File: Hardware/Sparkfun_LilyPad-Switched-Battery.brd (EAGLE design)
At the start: 31.9 x 30 mm, 13 parts

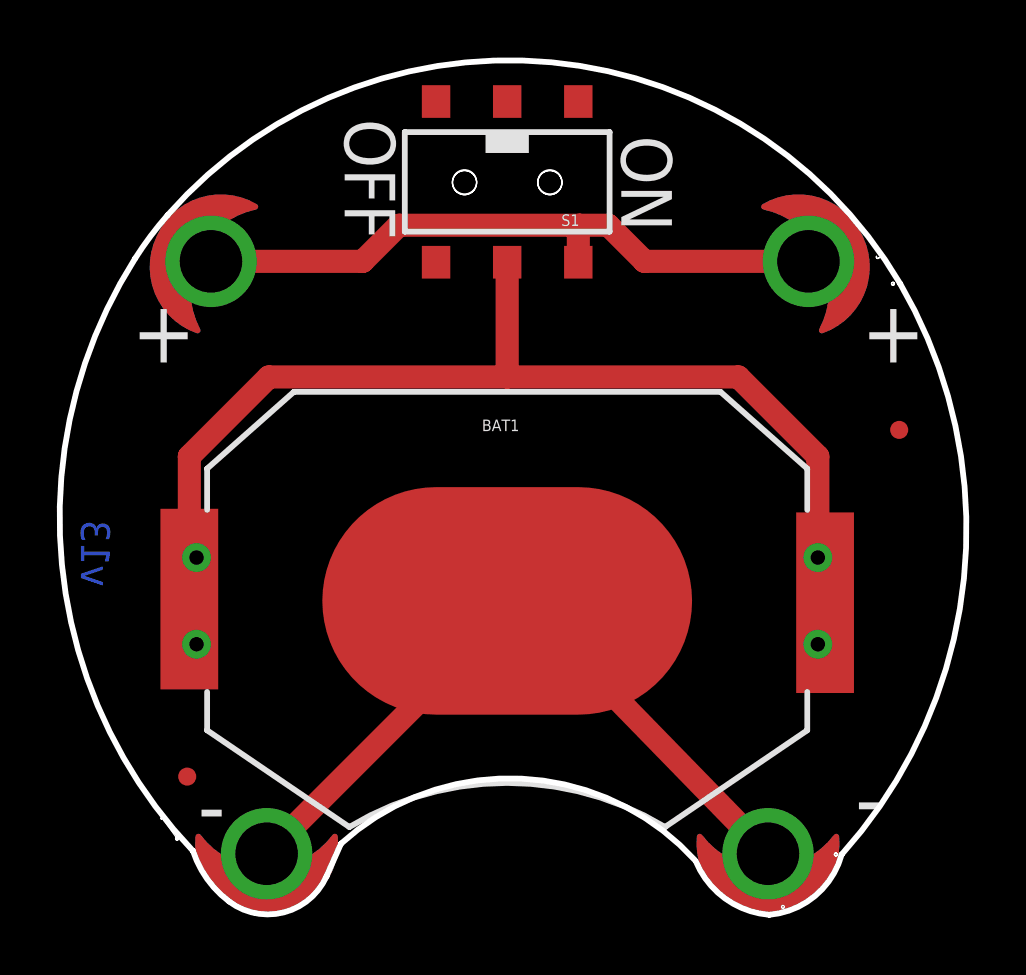
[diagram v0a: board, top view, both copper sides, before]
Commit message: Approved DRC errors
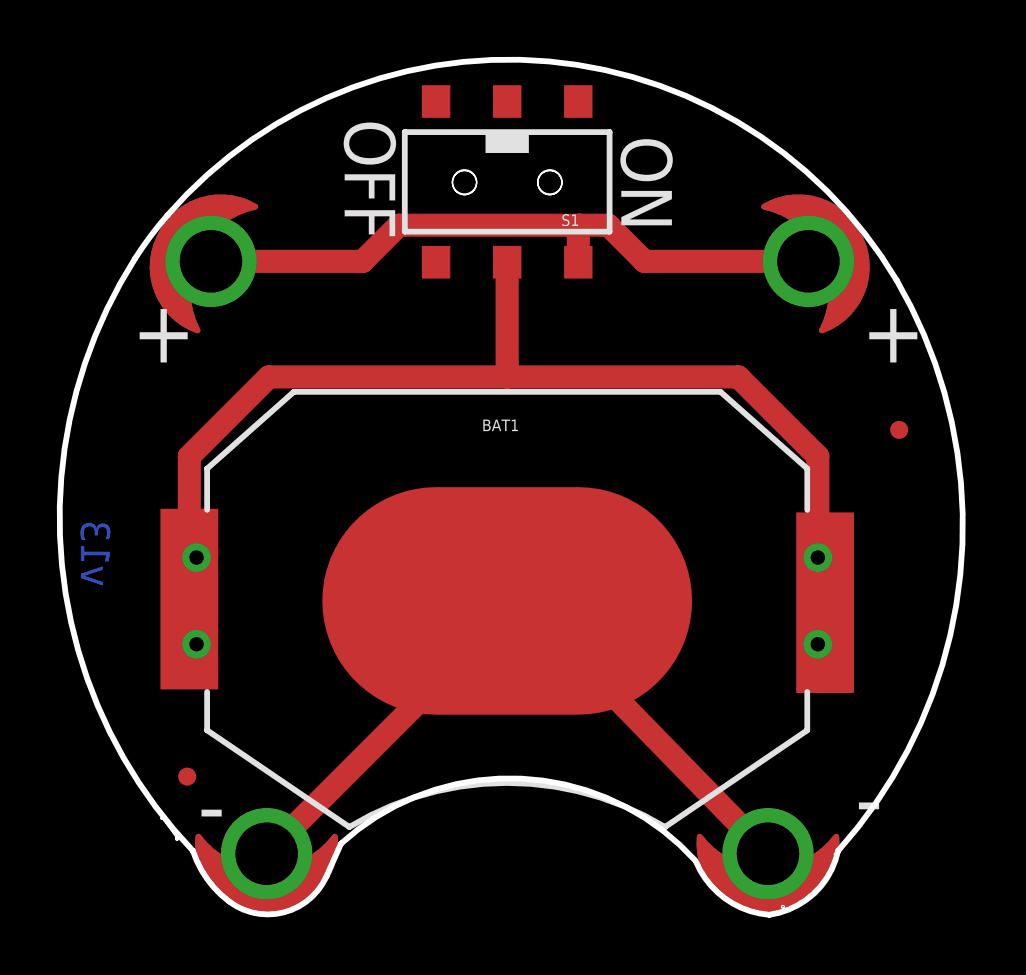
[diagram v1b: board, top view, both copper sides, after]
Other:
- board size 31.9 x 30 mm -> 31.7 x 30.1 mm
